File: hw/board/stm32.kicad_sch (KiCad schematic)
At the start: 12 parts, among them J1 Conn_ARM_JTAG_SWD_10, SW1 TSB008A2526A, SW2 TSB008A2526A, U1 STM32F302CBTx

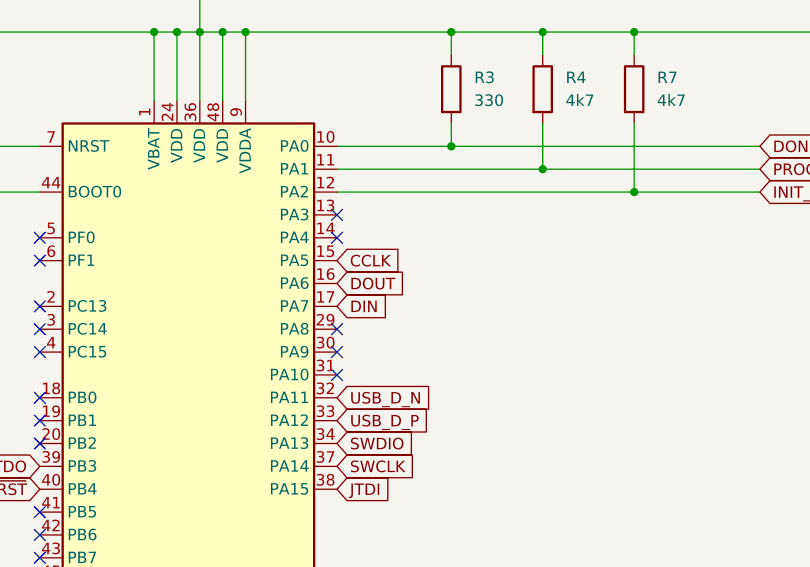
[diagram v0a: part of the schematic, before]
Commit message: Updated net names for SPI bitstream upload
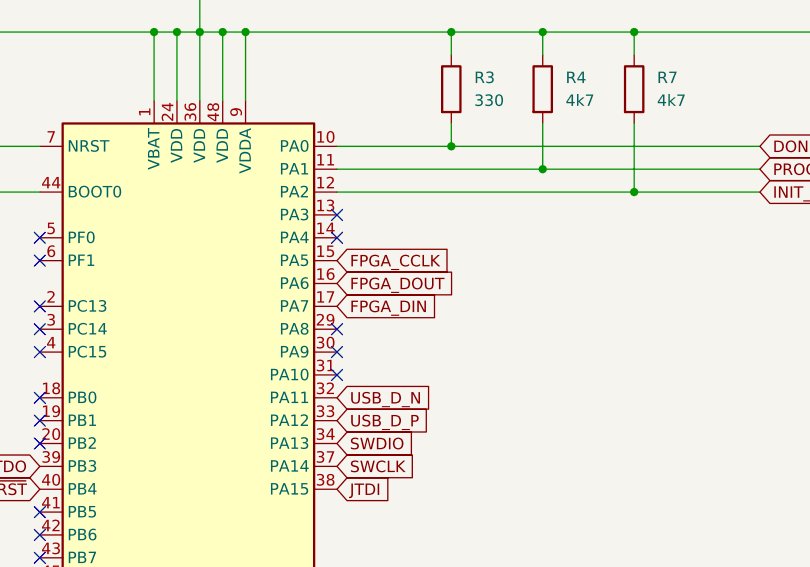
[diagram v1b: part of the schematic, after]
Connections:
- net CCLK renamed FPGA_CCLK
- net DIN renamed FPGA_DIN
- net DOUT renamed FPGA_DOUT
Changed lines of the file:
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@@
 		)
 	)
-	(global_label "DIN"
+	(global_label "FPGA_DIN"
 		(shape input)
 		(at 157.48 71.12 0)
@@
 		)
 		(property "Intersheetrefs" "${INTERSHEET_REFS}"
-			(at 163.6705 71.12 0)
+			(at 169.3553 71.12 0)
 			(effects
 				(font
@@
 		)
 	)
-	(global_label "DOUT"
+	(global_label "FPGA_DOUT"
 		(shape input)
 		(at 157.48 68.58 0)
@@
 		)
 		(property "Intersheetrefs" "${INTERSHEET_REFS}"
-			(at 165.3638 68.58 0)
-			(effects
-				(font
-					(size 1.27 1.27)
-				)
-				(justify left)
-				(hide yes)
-			)
-		)
-	)
-	(global_label "CCLK"
+			(at 171.0486 68.58 0)
+			(effects
+				(font
+					(size 1.27 1.27)
+				)
+				(justify left)
+				(hide yes)
+			)
+		)
+	)
+	(global_label "FPGA_CCLK"
 		(shape input)
 		(at 157.48 66.04 0)
@@
 		)
 		(property "Intersheetrefs" "${INTERSHEET_REFS}"
-			(at 165.3033 66.04 0)
-			(effects
-				(font
+			(at 170.9881 66.04 0)
+			(effects
+				(font

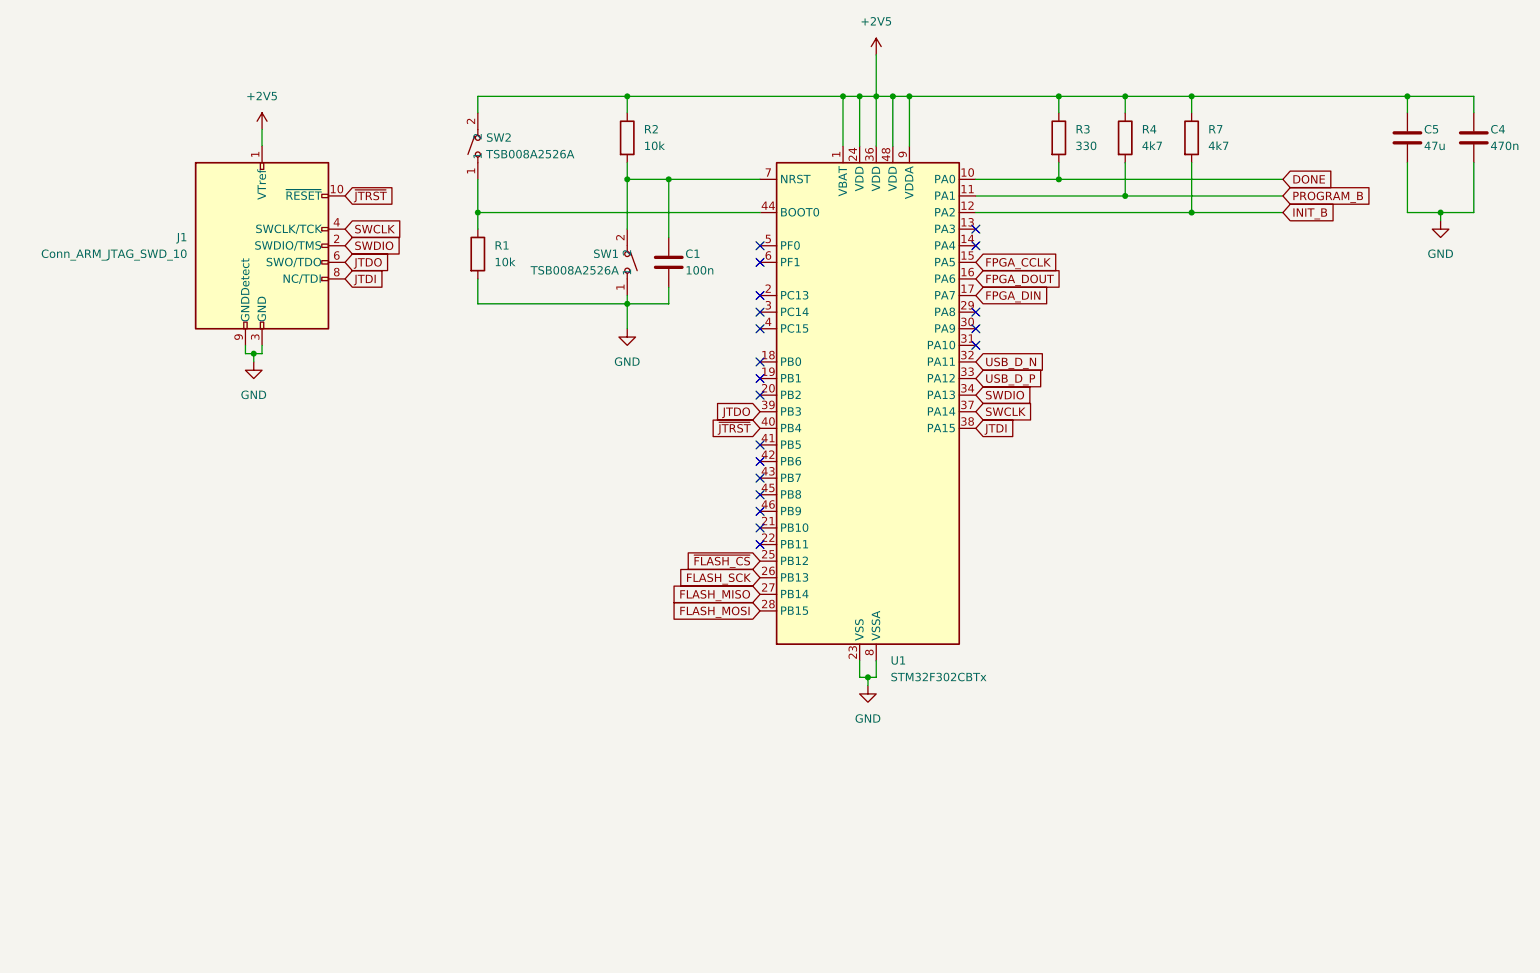
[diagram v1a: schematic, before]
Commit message: Reduced flash size
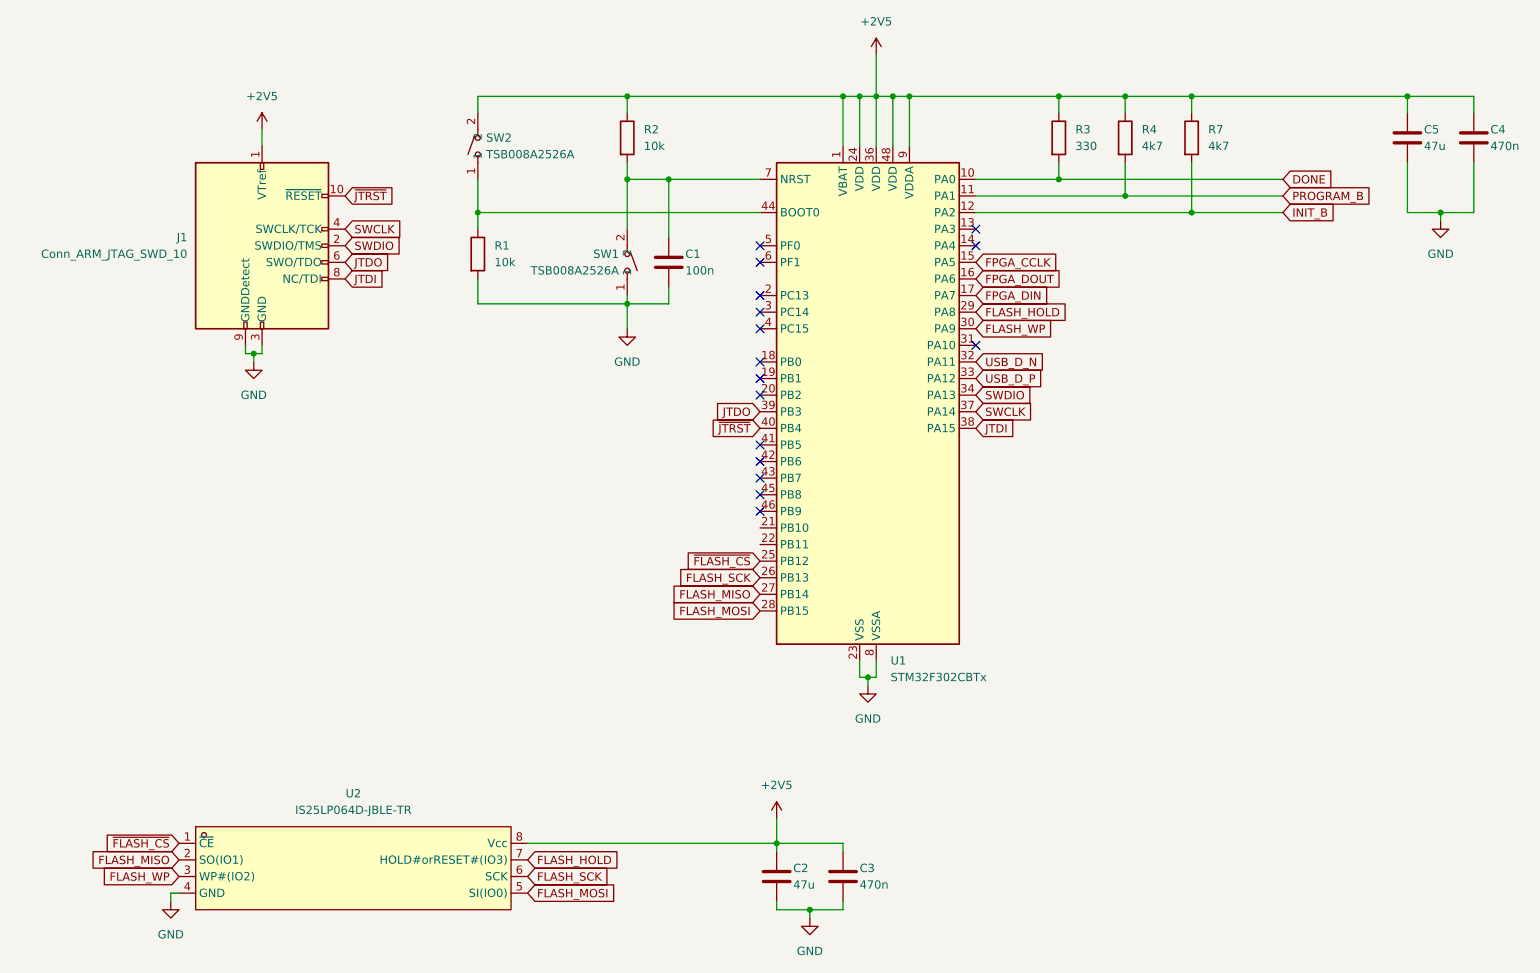
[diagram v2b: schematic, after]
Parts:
- added C2: 47u, Capacitor_SMD:C_0805_2012Metric, symbol Device:C
- added C3: 470n, Capacitor_SMD:C_0805_2012Metric, symbol Device:C
- added U2: IS25LP064D-JBLE-TR, EasyEDA:SOIC-8_L5.3-W5.3-P1.27-LS7.9-BL, symbol EasyEDA:IS25LP064D-JBLE-TR
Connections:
- net +2V5: now also C2.1, C3.1, U2.8 (Vcc)
- net FLASH_MISO: now also U2.2 (SO(IO1))
- net FLASH_MOSI: now also U2.5 (SI(IO0))
- net FLASH_SCK: now also U2.6 (SCK)
- net GND: now also C2.2, C3.2, U2.4 (GND)
- net ~{FLASH_CS}: now also U2.1 (~{CE})
- net FLASH_HOLD: now reaches U1.29 (PA8)
- net FLASH_HOLD: now also U2.7 (HOLD#orRESET#(IO3))
- net FLASH_WP: now reaches U1.30 (PA9)
- net FLASH_WP: now also U2.3 (WP#(IO2))
- no-connect marks 20 -> 16
